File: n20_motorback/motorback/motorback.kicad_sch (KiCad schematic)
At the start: 10 parts, among them J1 Conn_01x03_Male, J2 Conn_01x01_Male, J3 Conn_01x01_Male, U1 DRV8837, U2 ATtiny13V-10SSU

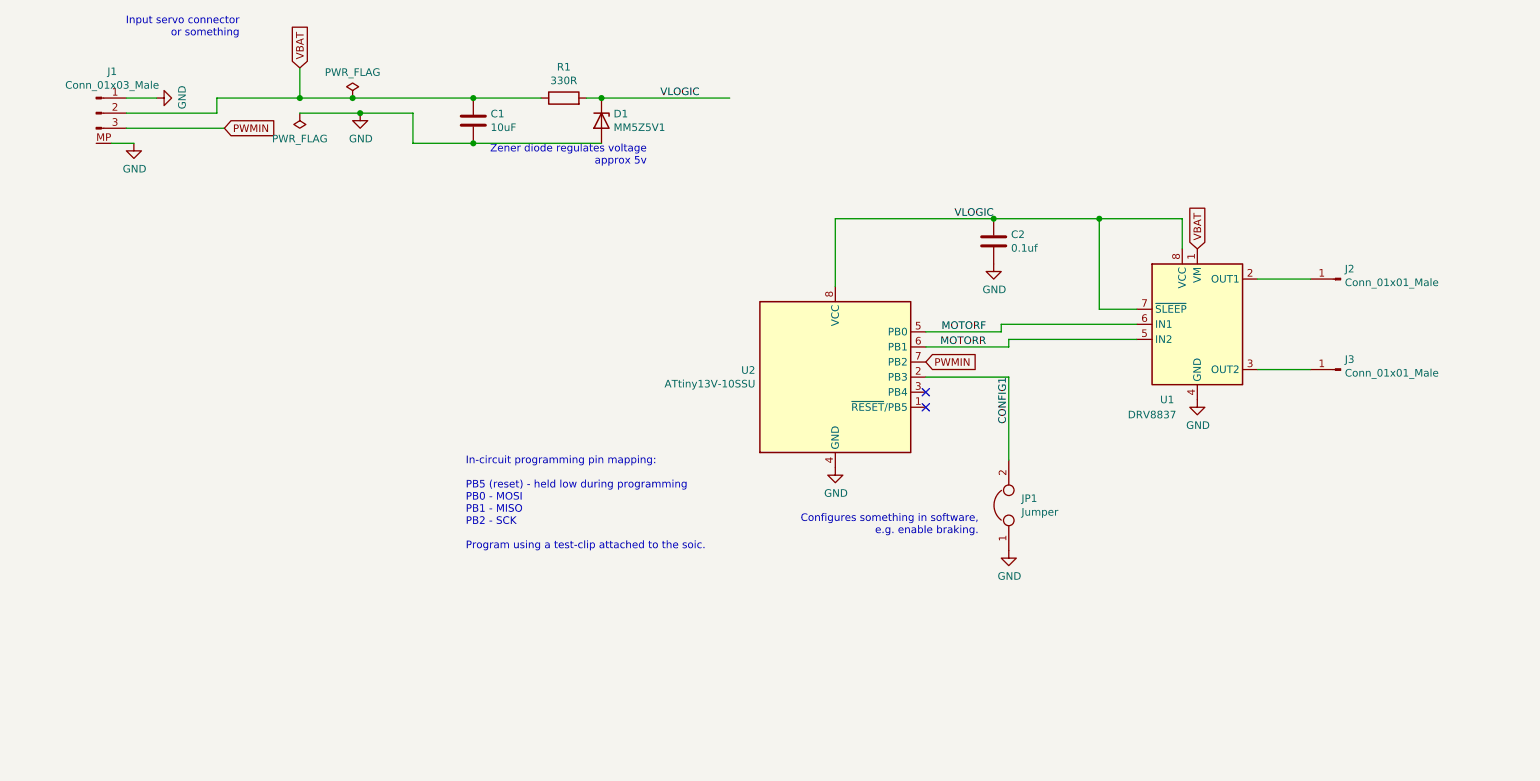
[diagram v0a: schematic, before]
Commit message: update to linear regulator
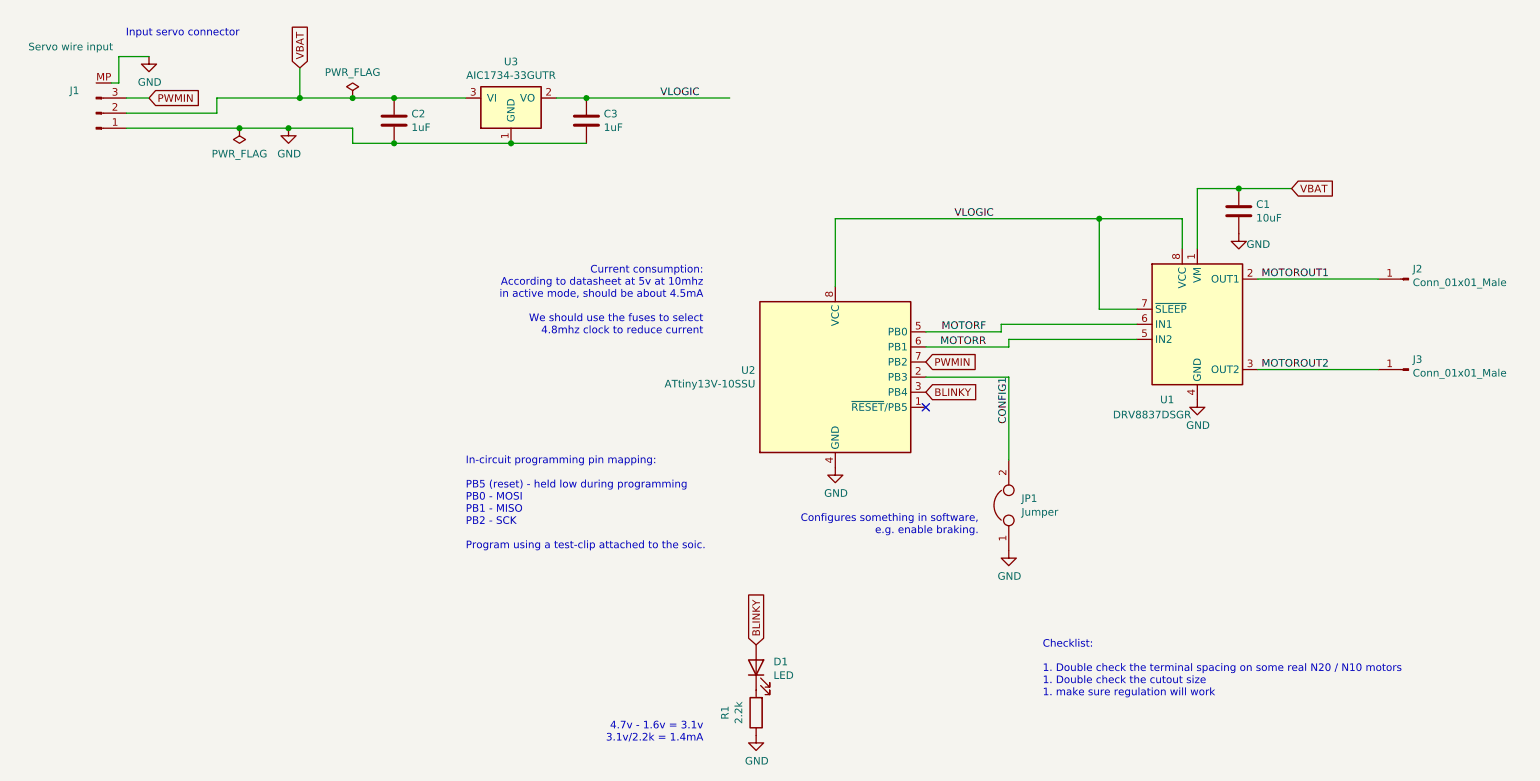
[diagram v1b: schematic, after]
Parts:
- removed D1: MM5Z5V1, Diode_SMD:D_SOD-523, symbol Device:D_Zener
- added C3: 1uF, Capacitor_SMD:C_0603_1608Metric, symbol Device:C
- added D1: LED, LED_SMD:LED_0603_1608Metric, symbol Device:LED
- added U3: AIC1734-33GUTR, Package_TO_SOT_SMD:SOT-23, symbol motorback:generic_regulator_GOI
- C2: value 0.1uf -> 1uF; LCSC C14663 -> (none)
- J1: value Conn_01x03_Male -> Servo wire input
- R1: value 330R -> 2.2k; LCSC C23138 -> (none)
- U1: value DRV8837 -> DRV8837DSGR
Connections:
- net GND: now also R1.1, C3.2, U3.1 (GND)
- net VBAT: now also C2.1, U3.3 (VI); no longer R1.1
- net VLOGIC: now also C3.1, U3.2 (VO); no longer C2.1, R1.2
- net MOTOROUT1: now reaches J2.1 (Pin_1), U1.2 (OUT1)
- net MOTOROUT2: now reaches J3.1 (Pin_1), U1.3 (OUT2)
- net BLINKY: now reaches U2.3 (PB4)
- net BLINKY: now also D1.2 (A)
- new net: D1.1 (K), R1.2
- no-connect marks 2 -> 1
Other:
- note added: "4.7v - 1.6v = 3.1v 3.1v/2.2k = 1.4mA"
- note added: "Checklist: 1. Double check the terminal spacing on some real N20 / N10 motors 1. Double check the cutout size 1. make sure regulation will work"
- note added: "Current consumption: According to datasheet at 5v at 10mhz in active mode, should be about 4.5mA We should use the fuses to select 4.8mhz clock to reduce current"
- note added: "Input servo connector"
- note removed: "Input servo connector or something"
- note removed: "Zener diode regulates voltage approx 5v"
- company: (none) -> Mark Robson
- title: (none) -> N20 motor back ESC
- moved on the sheet: J1, J2, J3

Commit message: misc update
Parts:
- C2, C3: LCSC (none) -> C15849
- D1: LCSC (none) -> C2286
- R1: value 2.2k -> 1k; LCSC (none) -> C21190
- U2: symbol MCU_Microchip_ATtiny:ATtiny13V-10SSU -> MCU_Microchip_ATtiny:ATtiny13A-SS; LCSC C40382 -> C14075
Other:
- note added: "3.3v - 1.6v = 1.7v 1.7v/1000 = 1.7mA"
- note added: "Current consumption: According to datasheet at 5v at 10mhz in active mode, should be about 4.5mA We could use the fuses to select 4.8mhz clock to reduce current"
- note removed: "4.7v - 1.6v = 3.1v 3.1v/2.2k = 1.4mA"
- note removed: "Current consumption: According to datasheet at 5v at 10mhz in active mode, should be about 4.5mA We should use the fuses to select 4.8mhz clock to reduce current"
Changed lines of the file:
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@@
     (effects (font (size 1.27 1.27)) (justify left bottom))
   )
-  (text "Current consumption:\nAccording to datasheet at 5v at 10mhz \nin active mode, should be about 4.5mA\n\nWe should use the fuses to select\n4.8mhz clock to reduce current\n"
-    (at 133.985 83.185 0)
-    (effects (font (size 1.27 1.27)) (justify right bottom))
-  )
-  (text "4.7v - 1.6v = 3.1v\n3.1v/2.2k = 1.4mA" (at 133.985 151.765 180)
+  (text "Current consumption:\nAccording to datasheet at 5v at 10mhz \nin active mode, should be about 4.5mA\n\nWe could use the fuses to select\n4.8mhz clock to reduce current\n"
+    (at 99.06 83.82 0)
+    (effects (font (size 1.27 1.27)) (justify left bottom))
+  )
+  (text "3.3v - 1.6v = 1.7v\n1.7v/1000 = 1.7mA" (at 133.985 151.765 180)
     (effects (font (size 1.27 1.27)) (justify right bottom))
   )
@@
     (in_bom yes) (on_board yes)
     (property "Reference" "R1" (id 0) (at 137.6488 146.685 90))
-    (property "Value" "2.2k" (id 1) (at 139.947 146.685 90))
+    (property "Value" "1k" (id 1) (at 139.947 146.685 90))
     (property "Footprint" "Resistor_SMD:R_0603_1608Metric" (id 2) (at 144.653 146.685 90)
       (effects (font (size 1.27 1.27)) hide)
@@
       (effects (font (size 1.27 1.27)) hide)
     )
-    (property "LCSC" "" (id 4) (at 142.875 146.685 0)
+    (property "LCSC" "C21190" (id 4) (at 142.875 146.685 0)
       (effects (font (size 1.27 1.27)) hide)
     )
@@
       (effects (font (size 1.27 1.27)) hide)
     )
+    (property "LCSC" "C2286" (id 4) (at 142.875 139.065 0)
+      (effects (font (size 1.27 1.27)) hide)
+    )
   )
   (symbol (lib_id "Device:C") (at 81.915 46.99 0) (unit 1)
@@
       (effects (font (size 1.27 1.27)) hide)
     )
-    (property "LCSC" "" (id 4) (at 81.915 46.99 0)
+    (property "LCSC" "C15849" (id 4) (at 81.915 46.99 0)
       (effects (font (size 1.27 1.27)) hide)
     )
@@
       (effects (font (size 1.27 1.27)) hide)
     )
-    (property "LCSC" "" (id 4) (at 114.3 46.99 0)
+    (property "LCSC" "C15849" (id 4) (at 114.3 46.99 0)
       (effects (font (size 1.27 1.27)) hide)
     )
@@
     )
   )
-  (symbol (lib_id "MCU_Microchip_ATtiny:ATtiny13V-10SSU") (at 156.21 90.17 0) (unit 1)
+  (symbol (lib_id "MCU_Microchip_ATtiny:ATtiny13A-SS") (at 156.21 90.17 0) (unit 1)
     (in_bom yes) (on_board yes)
     (property "Reference" "U2" (id 0) (at 142.748 89.0206 0)
@@
       (effects (font (size 1.27 1.27) italic) hide)
     )
-    (property "Datasheet" "http://ww1.microchip.com/downloads/en/DeviceDoc/doc2535.pdf" (id 3) (at 156.21 90.17 0)
-      (effects (font (size 1.27 1.27)) hide)
-    )
-    (property "LCSC" "C40382" (id 4) (at 156.21 90.17 0)
+    (property "Datasheet" "http://ww1.microchip.com/downloads/en/DeviceDoc/doc8126.pdf" (id 3) (at 156.21 90.17 0)
+      (effects (font (size 1.27 1.27)) hide)
+    )
+    (property "LCSC" "C14075" (id 4) (at 156.21 90.17 0)
       (effects (font (size 1.27 1.27)) hide)
     )
@@
     )
     (path "/668b33c0-eeaa-4f9d-b177-e9bb894eaa23"
-      (reference "R1") (unit 1) (value "2.2k") (footprint "Resistor_SMD:R_0603_1608Metric")
+      (reference "R1") (unit 1) (value "1k") (footprint "Resistor_SMD:R_0603_1608Metric")
     )
     (path "/17f044cf-d669-4296-9d52-0d1ba68a5a56"

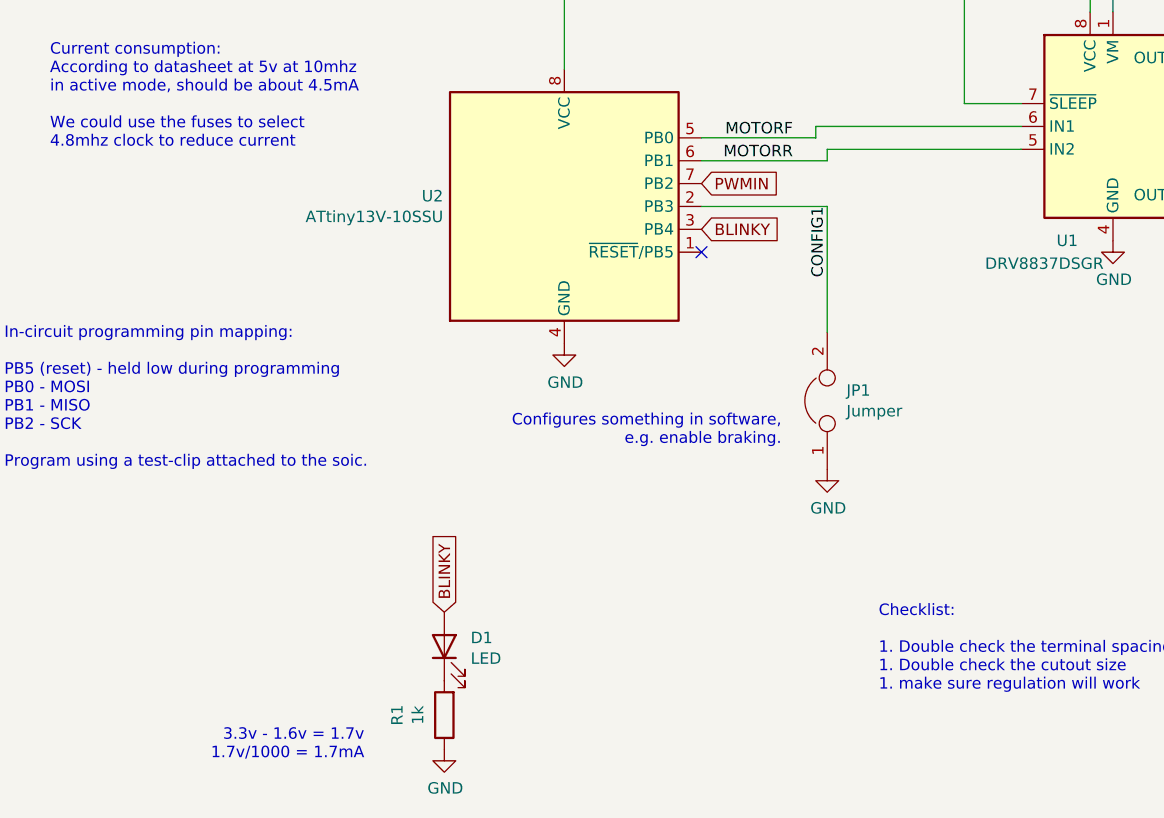
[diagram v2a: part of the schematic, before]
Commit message: dimension fixes and move cap
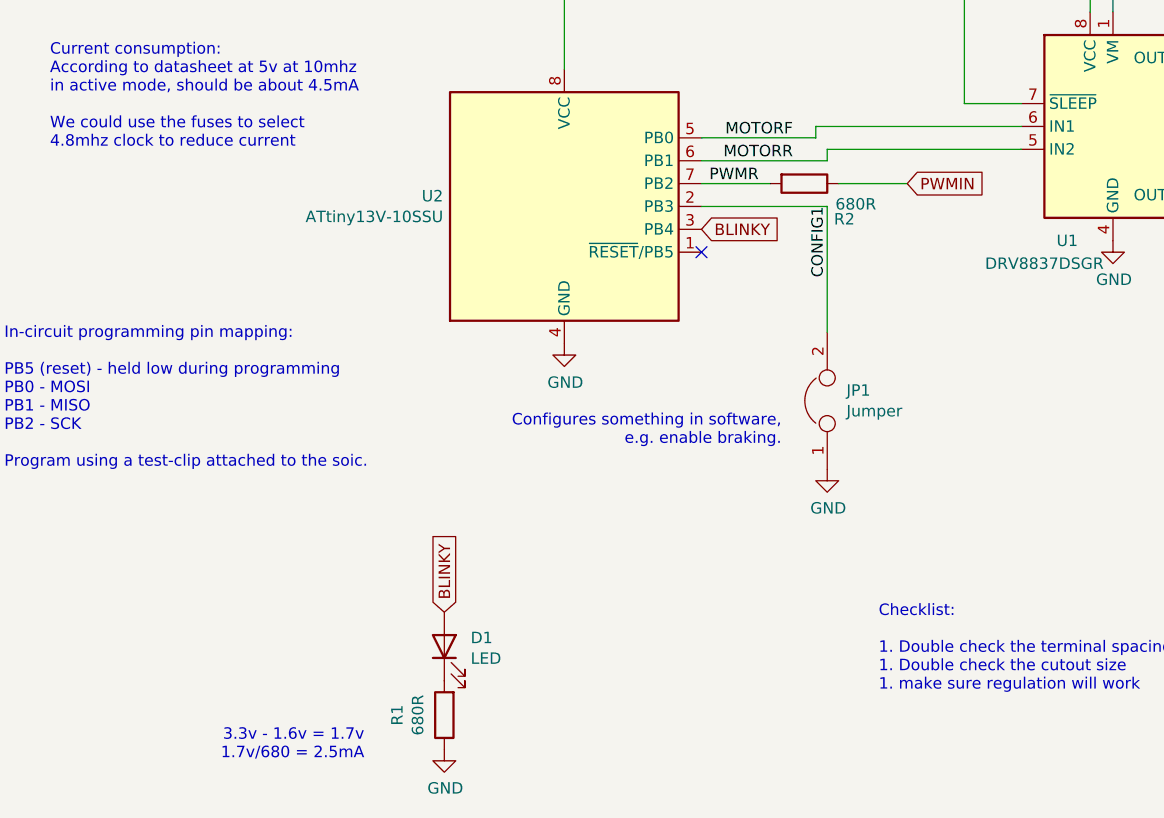
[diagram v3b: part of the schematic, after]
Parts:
- added R2: 680R, Resistor_SMD:R_0603_1608Metric, symbol Device:R
- R1: value 1k -> 680R; LCSC C21190 -> C23228
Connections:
- net PWMIN: now also R2.1; no longer U2.7 (PB2)
- new net PWMR: R2.2, U2.7 (PB2)
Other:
- note added: "3.3v - 1.6v = 1.7v 1.7v/680 = 2.5mA"
- note removed: "3.3v - 1.6v = 1.7v 1.7v/1000 = 1.7mA"
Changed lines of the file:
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@@
+    (stroke (width 0) (type solid) (color 0 0 0 0))
+  )
+  (wire (pts (xy 171.45 87.63) (xy 179.07 87.63))
     (stroke (width 0) (type solid) (color 0 0 0 0))
   )
@@
   )
   (wire (pts (xy 185.42 90.17) (xy 185.42 104.14))
+    (stroke (width 0) (type solid) (color 0 0 0 0))
+  )
+  (wire (pts (xy 186.69 87.63) (xy 194.31 87.63))
     (stroke (width 0) (type solid) (color 0 0 0 0))
   )
@@
     (effects (font (size 1.27 1.27)) (justify left bottom))
   )
-  (text "3.3v - 1.6v = 1.7v\n1.7v/1000 = 1.7mA" (at 133.985 151.765 180)
+  (text "3.3v - 1.6v = 1.7v\n1.7v/680 = 2.5mA" (at 133.985 151.765 180)
     (effects (font (size 1.27 1.27)) (justify right bottom))
   )
@@
     (effects (font (size 1.27 1.27)) (justify right bottom))
   )
+  (label "PWMR" (at 177.8 87.63 180)
+    (effects (font (size 1.27 1.27)) (justify right bottom))
+  )
   (label "MOTORF" (at 181.61 82.55 180)
     (effects (font (size 1.27 1.27)) (justify right bottom))
@@
     (effects (font (size 1.27 1.27)) (justify left))
   )
-  (global_label "PWMIN" (shape input) (at 171.45 87.63 0)    (property "Intersheet References" "${INTERSHEET_REFS}" (id 0) (at 0 0 0)
-      (effects (font (size 1.27 1.27)) hide)
-    )
-    (effects (font (size 1.27 1.27)) (justify left))
-  )
   (global_label "BLINKY" (shape input) (at 171.45 92.71 0)    (property "Intersheet References" "${INTERSHEET_REFS}" (id 0) (at 181.979 92.6306 0)
       (effects (font (size 1.27 1.27)) (justify left) hide)
@@
     (effects (font (size 1.27 1.27)) (justify left))
   )
+  (global_label "PWMIN" (shape input) (at 194.31 87.63 0)    (property "Intersheet References" "${INTERSHEET_REFS}" (id 0) (at 22.86 0 0)
+      (effects (font (size 1.27 1.27)) hide)
+    )
+    (effects (font (size 1.27 1.27)) (justify left))
+  )
   (global_label "VBAT" (shape input) (at 233.045 58.42 0)    (property "Intersheet References" "${INTERSHEET_REFS}" (id 0) (at 301.625 -158.75 0)
       (effects (font (size 1.27 1.27)) hide)
@@
     (in_bom yes) (on_board yes)
     (property "Reference" "R1" (id 0) (at 137.6488 146.685 90))
-    (property "Value" "1k" (id 1) (at 139.947 146.685 90))
+    (property "Value" "680R" (id 1) (at 139.947 146.685 90))
     (property "Footprint" "Resistor_SMD:R_0603_1608Metric" (id 2) (at 144.653 146.685 90)
       (effects (font (size 1.27 1.27)) hide)
@@
       (effects (font (size 1.27 1.27)) hide)
     )
-    (property "LCSC" "C21190" (id 4) (at 142.875 146.685 0)
+    (property "LCSC" "C23228" (id 4) (at 142.875 146.685 0)
+      (effects (font (size 1.27 1.27)) hide)
+    )
+  )
+  (symbol (lib_id "Device:R") (at 182.88 87.63 270) (unit 1)
+    (in_bom yes) (on_board yes)
+    (property "Reference" "R2" (id 0) (at 187.325 91.5862 90))
+    (property "Value" "680R" (id 1) (at 188.595 89.923 90))
+    (property "Footprint" "Resistor_SMD:R_0603_1608Metric" (id 2) (at 182.88 85.852 90)
+      (effects (font (size 1.27 1.27)) hide)
+    )
+    (property "Datasheet" "~" (id 3) (at 182.88 87.63 0)
+      (effects (font (size 1.27 1.27)) hide)
+    )
+    (property "LCSC" "C23228" (id 4) (at 182.88 87.63 0)
       (effects (font (size 1.27 1.27)) hide)
     )
@@
     )
     (path "/668b33c0-eeaa-4f9d-b177-e9bb894eaa23"
-      (reference "R1") (unit 1) (value "1k") (footprint "Resistor_SMD:R_0603_1608Metric")
+      (reference "R1") (unit 1) (value "680R") (footprint "Resistor_SMD:R_0603_1608Metric")
+    )
+    (path "/92a7a6ba-5e73-468d-b3fe-9c3572a32afb"
+      (reference "R2") (unit 1) (value "680R") (footprint "Resistor_SMD:R_0603_1608Metric")
     )
     (path "/17f044cf-d669-4296-9d52-0d1ba68a5a56"

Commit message: mod soic8 footprint, minor updates
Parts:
- U2: footprint Package_SO:SOIC-8_3.9x4.9mm_P1.27mm -> motorback:SOIC-8_shortpin1
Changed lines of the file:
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@@
       (effects (font (size 1.27 1.27)) (justify right))
     )
-    (property "Footprint" "Package_SO:SOIC-8_3.9x4.9mm_P1.27mm" (id 2) (at 156.21 90.17 0)
+    (property "Footprint" "motorback:SOIC-8_shortpin1" (id 2) (at 156.21 90.17 0)
       (effects (font (size 1.27 1.27) italic) hide)
     )
@@
     )
     (path "/b27661b9-3bfb-4ac3-8d24-bfaa37326f5c"
-      (reference "U2") (unit 1) (value "ATtiny13V-10SSU") (footprint "Package_SO:SOIC-8_3.9x4.9mm_P1.27mm")
+      (reference "U2") (unit 1) (value "ATtiny13V-10SSU") (footprint "motorback:SOIC-8_shortpin1")
     )
     (path "/28a3a09c-94bf-4dc1-a2bc-cc4a3444516d"

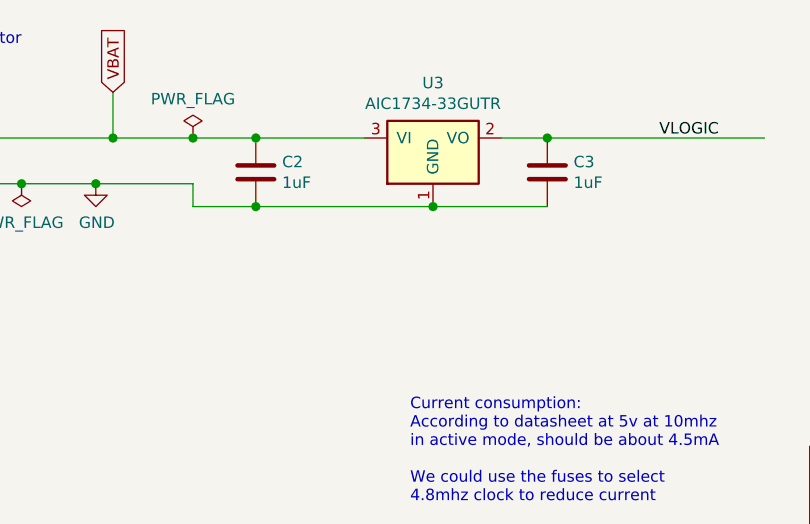
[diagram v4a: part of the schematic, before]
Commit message: use some 0402 caps; fix missing route from led resistor
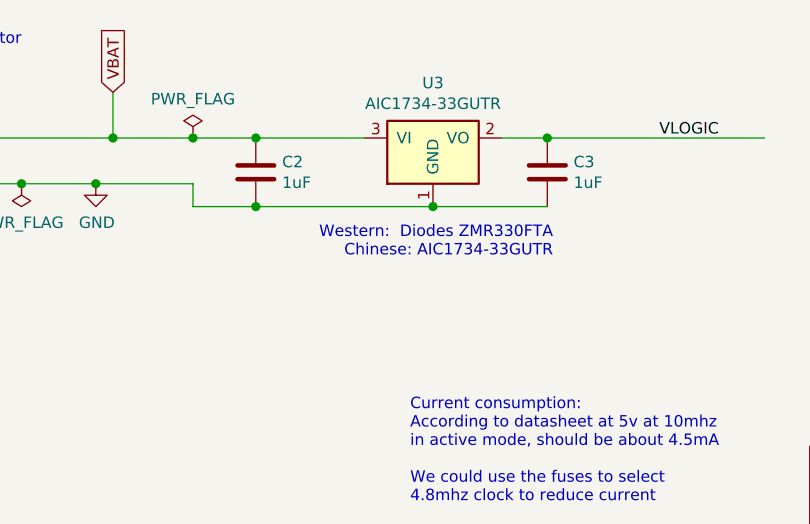
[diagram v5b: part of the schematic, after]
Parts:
- C2, C3: footprint Capacitor_SMD:C_0603_1608Metric -> Capacitor_SMD:C_0402_1005Metric
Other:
- note added: "Western: Diodes ZMR330FTA Chinese: AIC1734-33GUTR"
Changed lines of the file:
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@@
     (effects (font (size 1.27 1.27)) (justify left bottom))
+  )
+  (text "Western:  Diodes ZMR330FTA \nChinese: AIC1734-33GUTR"
+    (at 114.935 56.515 0)
+    (effects (font (size 1.27 1.27)) (justify right bottom))
   )
   (text "3.3v - 1.6v = 1.7v\n1.7v/680 = 2.5mA" (at 133.985 151.765 180)
@@
       (effects (font (size 1.27 1.27)) (justify left))
     )
-    (property "Footprint" "Capacitor_SMD:C_0603_1608Metric" (id 2) (at 82.8802 50.8 0)
+    (property "Footprint" "Capacitor_SMD:C_0402_1005Metric" (id 2) (at 82.8802 50.8 0)
       (effects (font (size 1.27 1.27)) hide)
     )
@@
       (effects (font (size 1.27 1.27)) (justify left))
     )
-    (property "Footprint" "Capacitor_SMD:C_0603_1608Metric" (id 2) (at 115.2652 50.8 0)
+    (property "Footprint" "Capacitor_SMD:C_0402_1005Metric" (id 2) (at 115.2652 50.8 0)
       (effects (font (size 1.27 1.27)) hide)
     )
@@
     )
     (path "/4f655001-cda0-4dbf-9ff7-65a9a8eac189"
-      (reference "C2") (unit 1) (value "1uF") (footprint "Capacitor_SMD:C_0603_1608Metric")
+      (reference "C2") (unit 1) (value "1uF") (footprint "Capacitor_SMD:C_0402_1005Metric")
     )
     (path "/b0a3ef47-4e9d-4c0a-897e-8ea5dc1d59c4"
-      (reference "C3") (unit 1) (value "1uF") (footprint "Capacitor_SMD:C_0603_1608Metric")
+      (reference "C3") (unit 1) (value "1uF") (footprint "Capacitor_SMD:C_0402_1005Metric")
     )
     (path "/5ba091cf-da2a-456f-9323-0ee75faa2288"
